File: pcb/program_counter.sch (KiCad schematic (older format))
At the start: 13 parts

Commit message: flash mem
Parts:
- removed U? (x5): 74LS08, symbol 74xx:74LS08
- removed U? (x2): 74LS32, symbol 74xx:74LS32
- added U?: SST39VF401C-70-4I-EKE-T, symbol nand2tetris:SST39VF401C-70-4I-EKE-T
- added U? (x5): 74LS08, symbol 74xx:74LS08
- added U? (x2): 74LS32, symbol 74xx:74LS32
- added U?: SN74LVCH16374A, symbol nand2tetris:SN74LVCH16374A
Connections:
- net gtz: now also U?.2
- net ins0: now also U?.2, U?.29 (DQ0)
- net ins1: now also U?.2, U?.31 (DQ1)
- net ins2: now also U?.2, U?.33 (DQ2)
- net insa: now also U?.2
- net jmp: now also U?.3
- net ltz: now also U?.1
- net nzr: now also U?.1
- net zr: now also U?.1
- new net: U?.1, U?.3 (x4)
- new net: U?.2, U?.3 (x2)
- new net ins10: U?.34 (DQ10)
- new net ins11: U?.36 (DQ11)
- new net ins12: U?.39 (DQ12)
- new net ins13: U?.41 (DQ13)
- new net ins14: U?.43 (DQ14)
- new net ins15: U?.45 (DQ15)
- new net ins3: U?.35 (DQ3)
- new net ins4: U?.38 (DQ4)
- new net ins5: U?.40 (DQ5)
- new net ins6: U?.42 (DQ6)
- new net ins7: U?.44 (DQ7)
- new net ins8: U?.30 (DQ8)
- new net ins9: U?.32 (DQ9)
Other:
- moved on the sheet: U?

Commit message: pc wip
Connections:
- net GND: now also U?.10 (GND), U?.15 (GND), U?.21 (GND), U?.27 (VSS), U?.28 (GND), U?.34 (GND), U?.39 (GND), U?.4 (GND), U?.45 (GND), U?.46 (VSS)
- net VCC: now also U?.18 (VCC), U?.31 (VCC), U?.37 (VDD), U?.42 (VCC), U?.7 (VCC)
- net clk: now also U?.25 (2CLK), U?.48 (1D2)
- net pc0: now also U?.46 (1D1)
- net pc1: now also U?.48 (1D2)
- net pc10: now also U?.33 (2D3)
- net pc11: now also U?.32 (2D4)
- net pc12: now also U?.30 (2D5)
- net pc13: now also U?.29 (2D6)
- net pc14: now also U?.27 (2D7)
- net pc15: now also U?.26 (2D8)
- net pc2: now also U?.44 (1D3)
- net pc3: now also U?.43 (1D4)
- net pc4: now also U?.41 (1D5)
- net pc5: now also U?.40 (1D6)
- net pc6: now also U?.38 (1D7)
- net pc7: now also U?.37 (1D8)
- net pc8: now also U?.36 (2D1)
- net pc9: now also U?.35 (2D2)
- net at U?.1 (A15): now also U?.23 (2Q8)
- net high: now reaches U?.15 (RY/BY)
- net at U?.18 (A7): now also U?.12 (1Q8)
- net at U?.19 (A6): now also U?.11 (1Q7)
- net at U?.2 (A14): now also U?.22 (2Q7)
- net at U?.20 (A5): now also U?.9 (1Q6)
- net at U?.21 (A4): now also U?.8 (1Q5)
- net at U?.22 (A3): now also U?.6 (1Q4)
- net at U?.23 (A2): now also U?.5 (1Q3)
- net at U?.24 (A1): now also U?.3 (1Q2)
- net at U?.25 (A0): now also U?.2 (1Q1)
- net at U?.3 (A13): now also U?.20 (2Q6)
- net at U?.4 (A12): now also U?.19 (2Q5)
- net at U?.5 (A11): now also U?.17 (2Q4)
- net at U?.6 (A10): now also U?.16 (2Q3)
- net at U?.7 (A9): now also U?.14 (2Q2)
- net at U?.8 (A8): now also U?.13 (2Q1)
- net low: now reaches U?.1 (1~OE~)
- net low: now also U?.24 (2~OE~)
- no-connect marks 1 -> 8
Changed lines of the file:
@@
 	1    0    0    -1
 $EndComp
+Wire Wire Line
+	2800 4450 3350 4450
+Wire Wire Line
+	2800 4550 3350 4550
+Wire Wire Line
+	2800 4650 3350 4650
+Wire Wire Line
+	2800 4750 3350 4750
+Wire Wire Line
+	2800 4850 3350 4850
+Wire Wire Line
+	2800 4950 3350 4950
+Wire Wire Line
+	2800 5050 3350 5050
+Wire Wire Line
+	2800 5150 3350 5150
+Wire Wire Line
+	2800 5250 3350 5250
+Wire Wire Line
+	2800 5350 3350 5350
+Wire Wire Line
+	2800 5450 3350 5450
+Wire Wire Line
+	2800 5550 3350 5550
+Wire Wire Line
+	2800 5650 3350 5650
+Wire Wire Line
+	2800 5750 3350 5750
+Wire Wire Line
+	2800 5850 3350 5850
+Wire Wire Line
+	2800 5950 3350 5950
+NoConn ~ 3350 6050
+NoConn ~ 3350 6150
+Wire Wire Line
+	1850 6850 1950 6850
+Connection ~ 1950 6850
+Wire Wire Line
+	1950 6850 2050 6850
+Connection ~ 2050 6850
+Wire Wire Line
+	2050 6850 2150 6850
+Connection ~ 2150 6850
+Wire Wire Line
+	2150 6850 2250 6850
+Connection ~ 2250 6850
+Wire Wire Line
+	2250 6850 2350 6850
+Connection ~ 2350 6850
+Wire Wire Line
+	2350 6850 2450 6850
+Connection ~ 2450 6850
+Wire Wire Line
+	2450 6850 2550 6850
+$Comp
+L power:GND #PWR?
+U 1 1 5CDE2311
+P 2150 6950
+F 0 "#PWR?" H 2150 6700 50  0001 C CNN
+F 1 "GND" H 2155 6777 50  0000 C CNN
+F 2 "" H 2150 6950 50  0001 C CNN
+F 3 "" H 2150 6950 50  0001 C CNN
+	1    2150 6950
+	1    0    0    -1
+$EndComp
+Wire Wire Line
+	2150 6850 2150 6950
+Wire Wire Line
+	4200 6700 4250 6700
+Wire Wire Line
+	4250 6700 4250 6850
+Connection ~ 4250 6700
+Wire Wire Line
+	4250 6700 4300 6700
+$Comp
+L power:GND #PWR?
+U 1 1 5CDFD324
+P 4250 6850
+F 0 "#PWR?" H 4250 6600 50  0001 C CNN
+F 1 "GND" H 4255 6677 50  0000 C CNN
+F 2 "" H 4250 6850 50  0001 C CNN
+F 3 "" H 4250 6850 50  0001 C CNN
+	1    4250 6850
+	1    0    0    -1
+$EndComp
+Wire Wire Line
+	2050 4250 2150 4250
+Connection ~ 2150 4250
+Wire Wire Line
+	2150 4250 2250 4250
+Connection ~ 2250 4250
+Wire Wire Line
+	2250 4250 2350 4250
+Wire Wire Line
+	2250 4250 2250 4050
+Wire Wire Line
+	4150 4250 4150 4050
+$Comp
+L power:VCC #PWR?
+U 1 1 5CE19CDE
+P 2250 4050
+F 0 "#PWR?" H 2250 3900 50  0001 C CNN
+F 1 "VCC" H 2267 4223 50  0000 C CNN
+F 2 "" H 2250 4050 50  0001 C CNN
+F 3 "" H 2250 4050 50  0001 C CNN
+	1    2250 4050
+	1    0    0    -1
+$EndComp
+$Comp
+L power:VCC #PWR?
+U 1 1 5CE1AB20
+P 4150 4050
+F 0 "#PWR?" H 4150 3900 50  0001 C CNN
+F 1 "VCC" H 4167 4223 50  0000 C CNN
+F 2 "" H 4150 4050 50  0001 C CNN
+F 3 "" H 4150 4050 50  0001 C CNN
+	1    4150 4050
+	1    0    0    -1
+$EndComp
+Wire Wire Line
+	1550 4450 1350 4450
+Wire Wire Line
+	1550 4550 1350 4550
+Wire Wire Line
+	1550 4650 1350 4650
+Wire Wire Line
+	1550 4750 1350 4750
+Wire Wire Line
+	1550 4850 1350 4850
+Wire Wire Line
+	1550 4950 1350 4950
+Wire Wire Line
+	1550 5050 1350 5050
+Wire Wire Line
+	1550 5150 1350 5150
+Wire Wire Line
+	1550 5250 1350 5250
+Wire Wire Line
+	1550 5350 1350 5350
+Wire Wire Line
+	1550 5450 1350 5450
+Wire Wire Line
+	1550 5550 1350 5550
+Wire Wire Line
+	1550 5650 1350 5650
+Wire Wire Line
+	1550 5750 1350 5750
+Wire Wire Line
+	1550 5850 1350 5850
+Wire Wire Line
+	1550 5950 1350 5950
+Text GLabel 1350 4450 0    50   Input ~ 0
+pc0
+Text GLabel 1350 4550 0    50   Input ~ 0
+pc1
+Text GLabel 1350 4650 0    50   Input ~ 0
+pc2
+Text GLabel 1350 4750 0    50   Input ~ 0
+pc3
+Text GLabel 1350 4850 0    50   Input ~ 0
+pc4
+Text GLabel 1350 4950 0    50   Input ~ 0
+pc5
+Text GLabel 1350 5050 0    50   Input ~ 0
+pc6
+Text GLabel 1350 5150 0    50   Input ~ 0
+pc7
+Text GLabel 1350 5250 0    50   Input ~ 0
+pc8
+Text GLabel 1350 5350 0    50   Input ~ 0
+pc9
+Text GLabel 1350 5450 0    50   Input ~ 0
+pc10
+Text GLabel 1350 5550 0    50   Input ~ 0
+pc11
+Text GLabel 1350 5650 0    50   Input ~ 0
+pc12
+Text GLabel 1350 5750 0    50   Input ~ 0
+pc13
+Text GLabel 1350 5850 0    50   Input ~ 0
+pc14
+Text GLabel 1350 5950 0    50   Input ~ 0
+pc15
+Text GLabel 1400 6150 0    50   Input ~ 0
+low
+Wire Wire Line
+	1550 6150 1400 6150
+Text GLabel 1150 6450 0    50   Input ~ 0
+clk
+Wire Wire Line
+	1150 6450 1500 6450
+Wire Wire Line
+	1550 6350 1500 6350
+Wire Wire Line
+	1500 6350 1500 6450
+Connection ~ 1500 6450
+Wire Wire Line
+	1500 6450 1550 6450
+Wire Wire Line
+	1550 6250 1550 6150
+Connection ~ 1550 6150
+NoConn ~ 4400 6700
+NoConn ~ 4500 6700
+NoConn ~ 4600 6700
+NoConn ~ 4700 6700
+NoConn ~ 4800 6700
+Text GLabel 4050 6800 3    50   Input ~ 0
+high
+Wire Wire Line
+	4050 6700 4050 6800
 $EndSCHEMATC

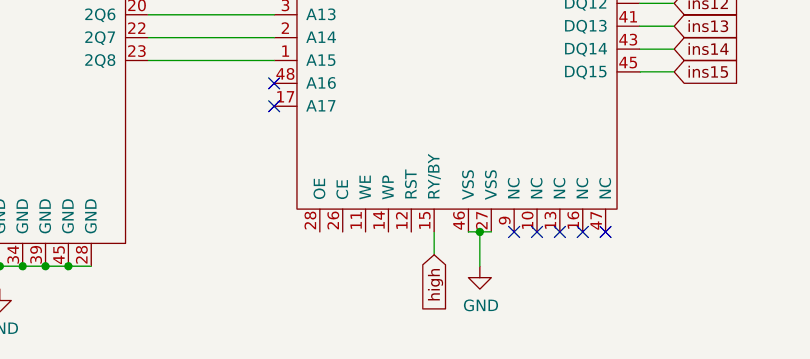
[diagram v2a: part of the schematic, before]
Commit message: program rom control
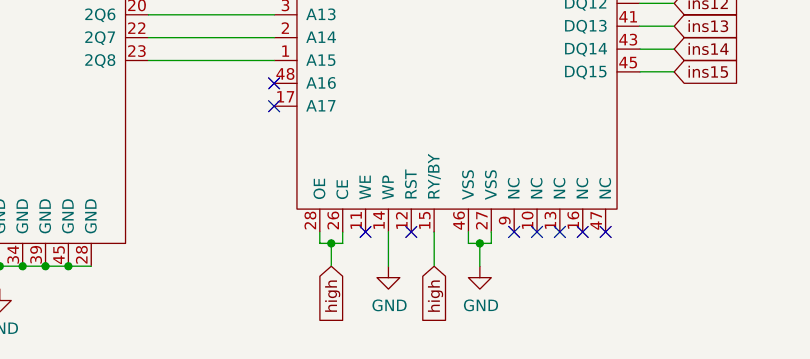
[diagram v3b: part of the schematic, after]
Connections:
- net GND: now also U?.14 (WP)
- net high: now also U?.26 (CE), U?.28 (OE)
- no-connect marks 8 -> 10
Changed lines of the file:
@@
 Wire Wire Line
 	2150 6850 2150 6950
-Wire Wire Line
-	4200 6700 4250 6700
-Wire Wire Line
-	4250 6700 4250 6850
-Connection ~ 4250 6700
-Wire Wire Line
-	4250 6700 4300 6700
 $Comp
 L power:GND #PWR?
@@
 NoConn ~ 4700 6700
 NoConn ~ 4800 6700
-Text GLabel 4050 6800 3    50   Input ~ 0
+Text GLabel 4050 6850 3    50   Input ~ 0
 high
 Wire Wire Line
-	4050 6700 4050 6800
+	3850 6700 3850 6850
+$Comp
+L power:GND #PWR?
+U 1 1 5CDD0642
+P 3850 6850
+F 0 "#PWR?" H 3850 6600 50  0001 C CNN
+F 1 "GND" H 3855 6677 50  0000 C CNN
+F 2 "" H 3850 6850 50  0001 C CNN
+F 3 "" H 3850 6850 50  0001 C CNN
+	1    3850 6850
+	1    0    0    -1
+$EndComp
+NoConn ~ 3950 6700
+NoConn ~ 3750 6700
+Wire Wire Line
+	3550 6700 3550 6750
+Wire Wire Line
+	3550 6750 3600 6750
+Wire Wire Line
+	3650 6750 3650 6700
+Wire Wire Line
+	3600 6750 3600 6850
+Connection ~ 3600 6750
+Wire Wire Line
+	3600 6750 3650 6750
+Text GLabel 3600 6850 3    50   Input ~ 0
+high
+Wire Wire Line
+	4200 6700 4200 6750
+Wire Wire Line
+	4200 6750 4250 6750
+Wire Wire Line
+	4300 6750 4300 6700
+Wire Wire Line
+	4250 6750 4250 6850
+Connection ~ 4250 6750
+Wire Wire Line
+	4250 6750 4300 6750
+Wire Wire Line
+	4050 6700 4050 6850
 $EndSCHEMATC
